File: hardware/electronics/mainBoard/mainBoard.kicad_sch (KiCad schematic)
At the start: 1 part, among them J1 Chassis Ground Strap

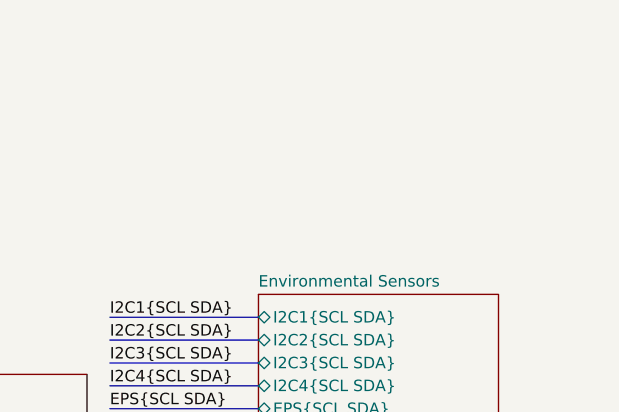
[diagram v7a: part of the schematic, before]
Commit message: added debugger sheet
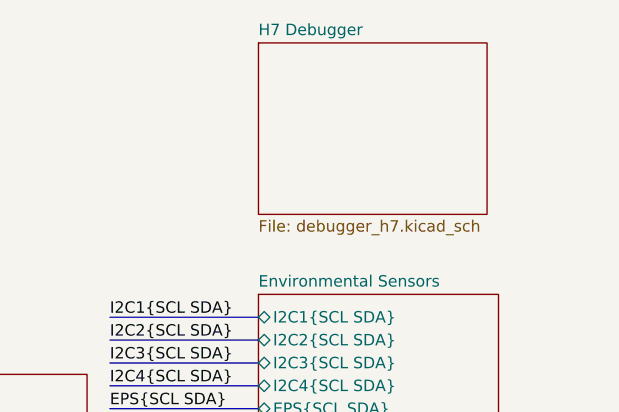
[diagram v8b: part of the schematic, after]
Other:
- added sheet H7 Debugger (debugger_h7.kicad_sch)
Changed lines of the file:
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@@
 			(project "mainBoard"
 				(path "/be16e32f-2ccf-4272-9ec7-94d5fe7a55e0"
-					(page "12")
+					(page "13")
 				)
 			)
@@
 				)
 			)
+		)
+	)
+	(sheet
+		(at 177.8 31.75)
+		(size 25.4 19.05)
+		(exclude_from_sim no)
+		(in_bom yes)
+		(on_board yes)
+		(dnp no)
+		(fields_autoplaced yes)
+		(stroke
+			(width 0.1524)
+			(type solid)
+		)
+		(fill
+			(color 0 0 0 0.0000)
+		)
+		(property "Sheetname" "H7 Debugger"
+			(at 177.8 31.0384 0)
+			(effects
+				(font
+					(size 1.27 1.27)
+				)
+				(justify left bottom)
+			)
+		)
+		(property "Sheetfile" "debugger_h7.kicad_sch"
+			(at 177.8 51.3846 0)
+			(effects
+				(font
+					(size 1.27 1.27)
+				)
+				(justify left top)
+			)
+		)
+		(instances
+			(project "mainBoard"
+				(path "/be16e32f-2ccf-4272-9ec7-94d5fe7a55e0"
+					(page "12")
+				)
+			)
